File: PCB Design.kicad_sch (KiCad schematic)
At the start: 8 parts

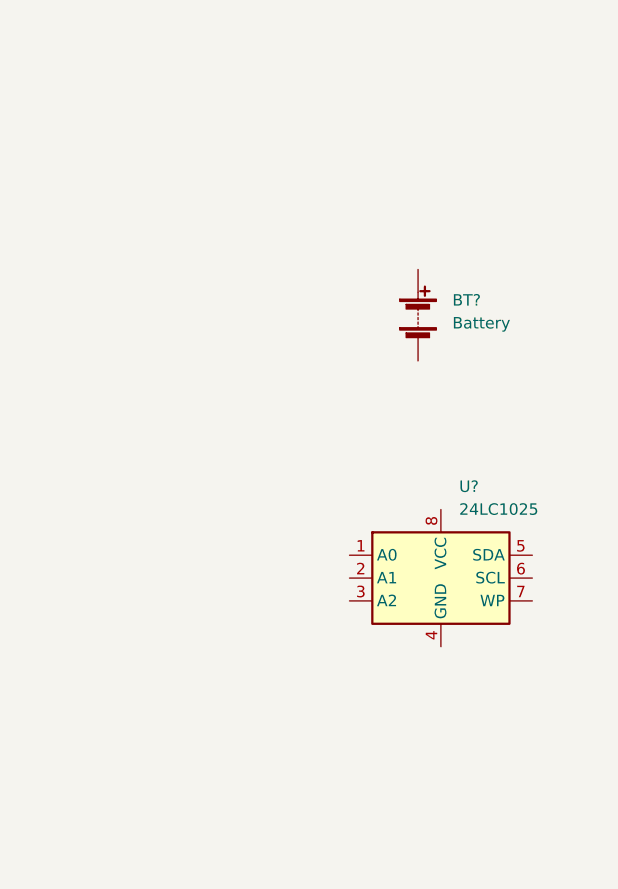
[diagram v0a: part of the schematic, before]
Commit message: add ATMEGA328P-AU from Digi-key library
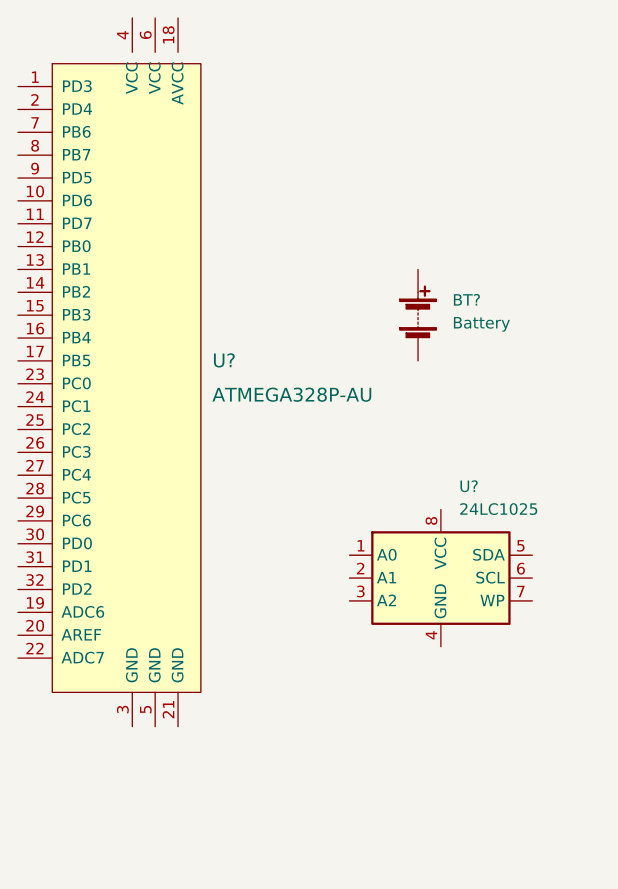
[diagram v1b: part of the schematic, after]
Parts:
- added U?: ATMEGA328P-AU, digikey-footprints:TQFP-32_7x7mm, symbol dk_Embedded-Microcontrollers:ATMEGA328P-AU
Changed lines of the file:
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@@
     (pin "8")
+  )
+  (symbol (lib_id "dk_Embedded-Microcontrollers:ATMEGA328P-AU") (at 52.07 92.71 0) (unit 1)
+    (in_bom yes) (on_board yes) (fields_autoplaced)
+    (property "Reference" "U?" (id 0) (at 60.96 90.17 0)
+      (effects (font (size 1.524 1.524)) (justify left))
+    )
+    (property "Value" "ATMEGA328P-AU" (id 1) (at 60.96 93.98 0)
+      (effects (font (size 1.524 1.524)) (justify left))
+    )
+    (property "Footprint" "digikey-footprints:TQFP-32_7x7mm" (id 2) (at 57.15 87.63 0)
+      (effects (font (size 1.524 1.524)) (justify left) hide)
+    )
+    (property "Datasheet" "http://www.microchip.com/mymicrochip/filehandler.aspx?ddocname=en608326" (id 3) (at 57.15 85.09 0)
+      (effects (font (size 1.524 1.524)) (justify left) hide)
+    )
+    (property "Digi-Key_PN" "ATMEGA328P-AU-ND" (id 4) (at 57.15 82.55 0)
+      (effects (font (size 1.524 1.524)) (justify left) hide)
+    )
+    (property "MPN" "ATMEGA328P-AU" (id 5) (at 57.15 80.01 0)
+      (effects (font (size 1.524 1.524)) (justify left) hide)
+    )
+    (property "Category" "Integrated Circuits (ICs)" (id 6) (at 57.15 77.47 0)
+      (effects (font (size 1.524 1.524)) (justify left) hide)
+    )
+    (property "Family" "Embedded - Microcontrollers" (id 7) (at 57.15 74.93 0)
+      (effects (font (size 1.524 1.524)) (justify left) hide)
+    )
+    (property "DK_Datasheet_Link" "http://www.microchip.com/mymicrochip/filehandler.aspx?ddocname=en608326" (id 8) (at 57.15 72.39 0)
+      (effects (font (size 1.524 1.524)) (justify left) hide)
+    )
+    (property "DK_Detail_Page" "/product-detail/en/microchip-technology/ATMEGA328P-AU/ATMEGA328P-AU-ND/1832260" (id 9) (at 57.15 69.85 0)
+      (effects (font (size 1.524 1.524)) (justify left) hide)
+    )
+    (property "Description" "IC MCU 8BIT 32KB FLASH 32TQFP" (id 10) (at 57.15 67.31 0)
+      (effects (font (size 1.524 1.524)) (justify left) hide)
+    )
+    (property "Manufacturer" "Microchip Technology" (id 11) (at 57.15 64.77 0)
+      (effects (font (size 1.524 1.524)) (justify left) hide)
+    )
+    (property "Status" "Active" (id 12) (at 57.15 62.23 0)
+      (effects (font (size 1.524 1.524)) (justify left) hide)
+    )
+    (pin "1")
+    (pin "10")
+    (pin "11")
+    (pin "12")
+    (pin "13")
+    (pin "14")
+    (pin "15")
+    (pin "16")
+    (pin "17")
+    (pin "18")
+    (pin "19")
+    (pin "2")
+    (pin "20")
+    (pin "21")
+    (pin "22")
+    (pin "23")
+    (pin "24")
+    (pin "25")
+    (pin "26")
+    (pin "27")
+    (pin "28")
+    (pin "29")
+    (pin "3")
+    (pin "30")
+    (pin "31")
+    (pin "32")
+    (pin "4")
+    (pin "5")
+    (pin "6")
+    (pin "7")
+    (pin "8")
+    (pin "9")
   )
   (symbol (lib_id "Device:LED") (at 205.74 77.47 0) (unit 1)
@@
       (reference "U?") (unit 1) (value "24LC1025") (footprint "")
     )
-  )
+    (path "/11816a99-511f-4707-8ba2-7dbc85864458"
+      (reference "U?") (unit 1) (value "ATMEGA328P-AU") (footprint "digikey-footprints:TQFP-32_7x7mm")
+    )
+  )

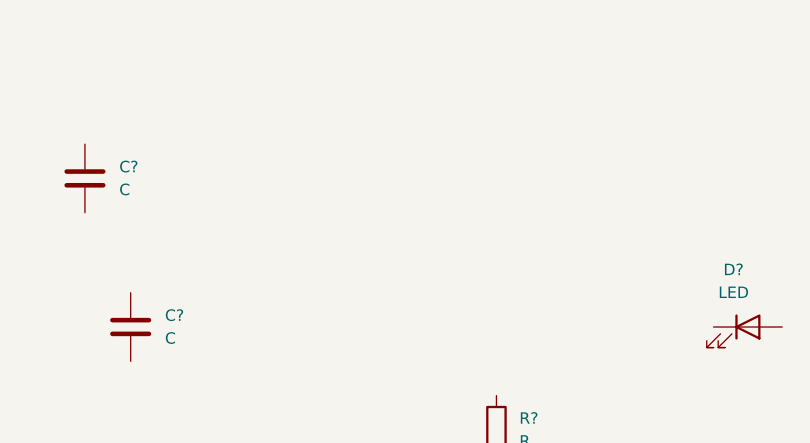
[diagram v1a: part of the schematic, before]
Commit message: add custom clock IC symbol
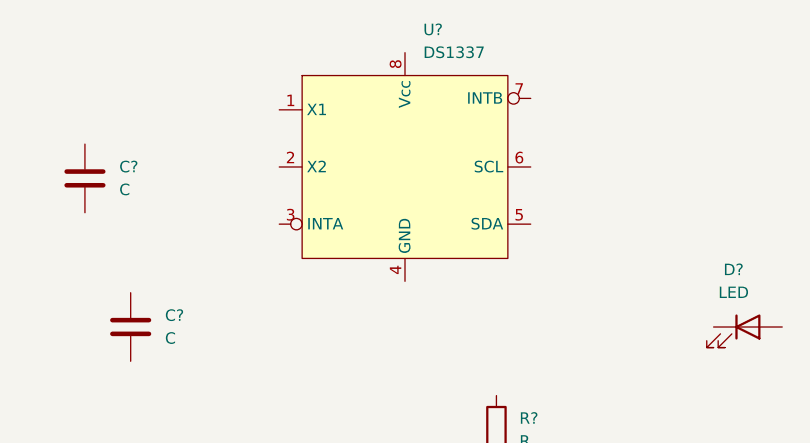
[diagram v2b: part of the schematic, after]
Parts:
- added U?: DS1337, symbol I2CRTC:DS1337
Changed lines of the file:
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@@
     (pin "2")
+  )
+  (symbol (lib_id "I2CRTC:DS1337") (at 167.64 59.69 0) (unit 1)
+    (in_bom yes) (on_board yes) (fields_autoplaced)
+    (property "Reference" "U?" (id 0) (at 169.6594 44.45 0)
+      (effects (font (size 1.27 1.27)) (justify left))
+    )
+    (property "Value" "DS1337" (id 1) (at 169.6594 46.99 0)
+      (effects (font (size 1.27 1.27)) (justify left))
+    )
+    (property "Footprint" "" (id 2) (at 167.64 59.69 0)
+      (effects (font (size 1.27 1.27)) hide)
+    )
+    (property "Datasheet" "" (id 3) (at 167.64 59.69 0)
+      (effects (font (size 1.27 1.27)) hide)
+    )
+    (pin "1")
+    (pin "2")
+    (pin "3")
+    (pin "4")
+    (pin "5")
+    (pin "6")
+    (pin "7")
+    (pin "8")
   )
   (symbol (lib_id "Device:C") (at 137.16 77.47 0) (unit 1)
@@
       (reference "U?") (unit 1) (value "ATMEGA328P-AU") (footprint "digikey-footprints:TQFP-32_7x7mm")
     )
+    (path "/b261580b-4179-4e44-80bf-c6d63aab43a1"
+      (reference "U?") (unit 1) (value "DS1337") (footprint "")
+    )
   )

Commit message: complete footprint association
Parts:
- added U2: 24LC1025, Package_SO:SOIC-8_5.23x5.23mm_P1.27mm, symbol Memory_EEPROM:24LC1025
- added Y1: Crystal 32MHz, Crystal:Crystal_SMD_MicroCrystal_CC7V-T1A-2Pin_3.2x1.5mm, symbol Device:Crystal
- added Y2: Crystal 16MHz, Crystal:Crystal_SMD_5032-2Pin_5.0x3.2mm_HandSoldering, symbol Device:Crystal
- BT1: renamed from BT?; value Battery -> Battery 3V; footprint (none) -> Connector_PinHeader_2.54mm:PinHeader_1x02_P2.54mm_Vertical
- C1, C2: renamed from C?; value C -> 22pF; footprint (none) -> Capacitor_SMD:C_0805_2012Metric_Pad1.18x1.45mm_HandSolder
- C3: renamed from C?; value C_Polarized -> 10uF; footprint (none) -> Capacitor_SMD:C_0805_2012Metric_Pad1.18x1.45mm_HandSolder
- D1: renamed from D?; footprint (none) -> LED_SMD:LED_0805_2012Metric_Pad1.15x1.40mm_HandSolder
- R1: renamed from R?; value R -> 330Ohm; footprint (none) -> Resistor_SMD:R_0805_2012Metric_Pad1.20x1.40mm_HandSolder
- R2: renamed from R?; value R -> 10KOhm; footprint (none) -> Resistor_SMD:R_0805_2012Metric_Pad1.20x1.40mm_HandSolder
- U1: renamed from U?; footprint (none) -> Package_SO:SOIC-8_5.23x5.23mm_P1.27mm
- U3: renamed from U?; footprint (none) -> Package_SO:SO-8_5.3x6.2mm_P1.27mm
- gave numbers to parts that had none: 1
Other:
- moved on the sheet: BT1, C1, C2, C3, D1, R1, R2, U1, U3, U4

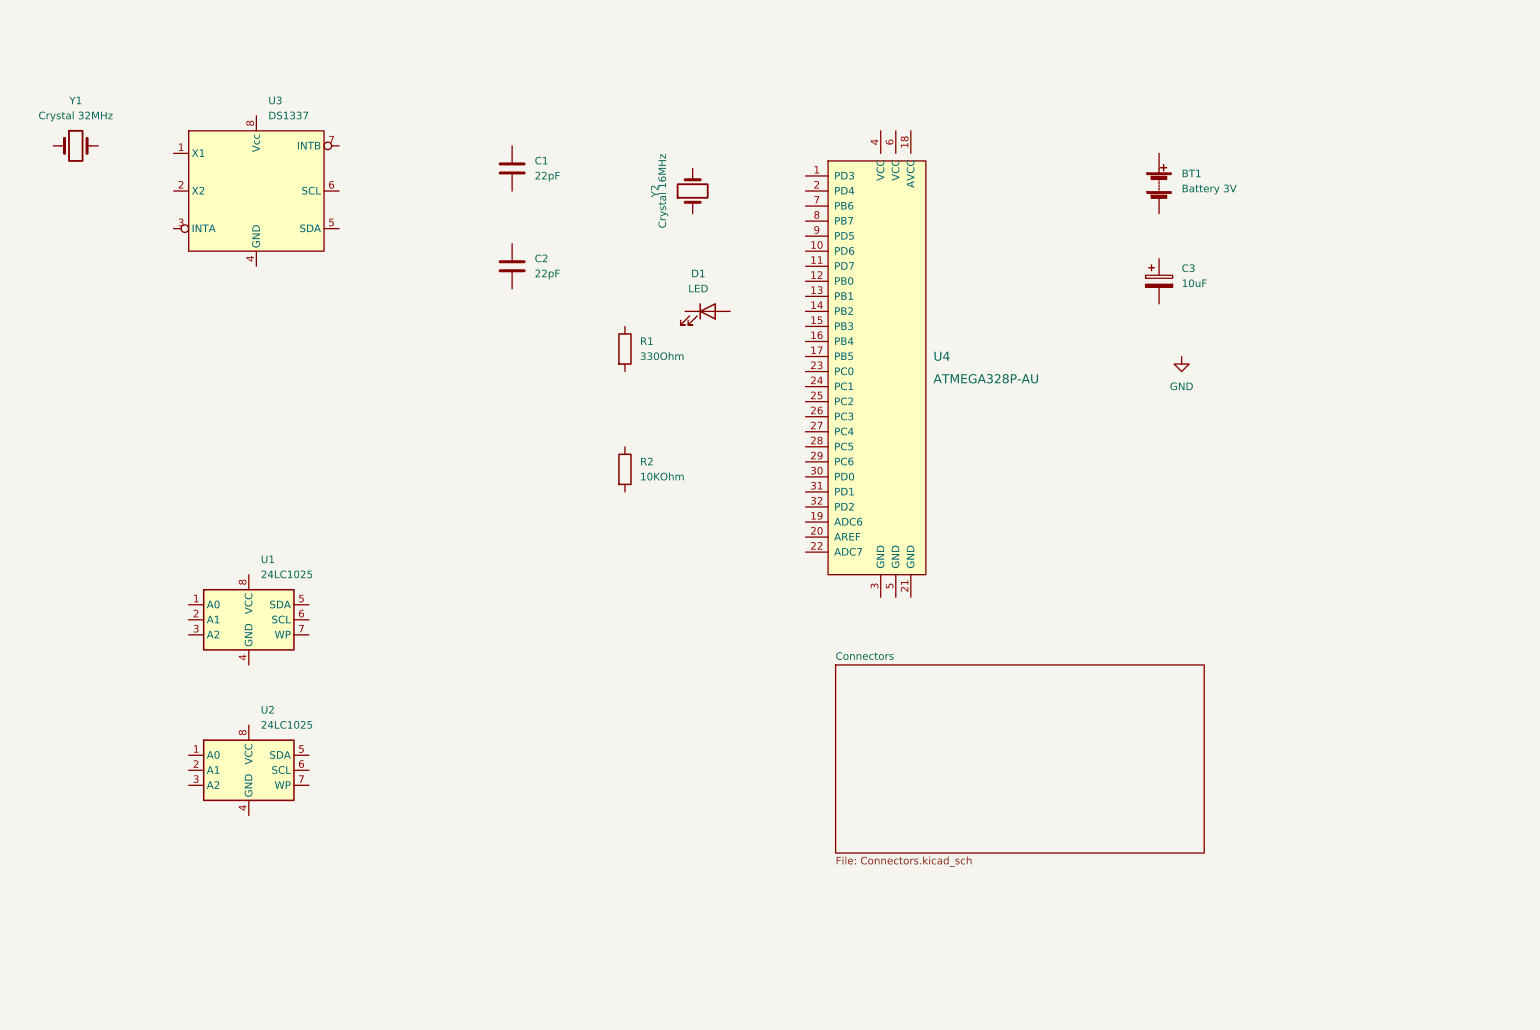
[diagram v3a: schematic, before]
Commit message: complete wiring in the root sheet
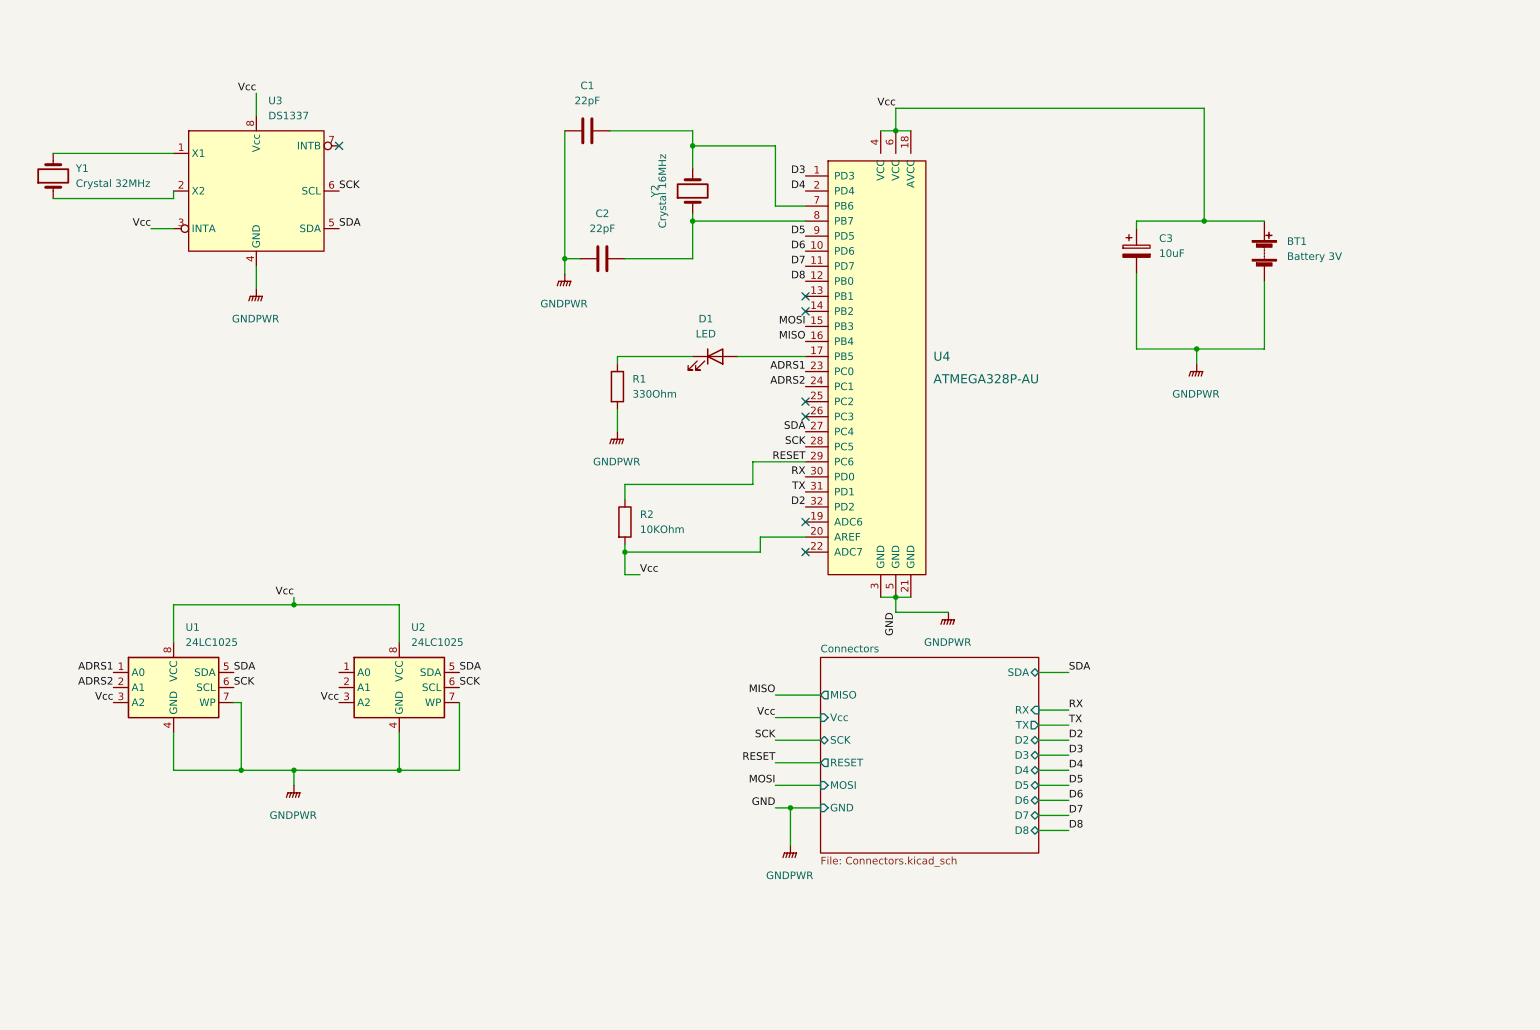
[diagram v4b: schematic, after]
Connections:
- net ADRS1: now reaches U1.1 (A0)
- net ADRS1: now also U4.23 (PC0)
- net ADRS2: now reaches U1.2 (A1)
- net ADRS2: now also U4.24 (PC1)
- net Vcc: now reaches U1.3 (A2)
- net Vcc: now also BT1.1 (+), C3.1, R2.2, U1.8 (VCC), U2.3 (A2), U2.8 (VCC), U3.3 (INTA), U3.8 (Vcc), U4.18 (AVCC), U4.20 (AREF), U4.4 (VCC), U4.6 (VCC)
- net GNDPWR: now reaches U1.4 (GND)
- net GNDPWR: now also BT1.2 (-), C1.1, C2.1, C3.2, R1.2, U1.7 (WP), U2.4 (GND), U2.7 (WP), U3.4 (GND), U4.21 (GND), U4.3 (GND), U4.5 (GND)
- net SDA: now reaches U1.5 (SDA)
- net SDA: now also U2.5 (SDA), U3.5 (SDA), U4.27 (PC4)
- net SCK: now reaches U1.6 (SCL)
- net SCK: now also U2.6 (SCL), U3.6 (SCL), U4.28 (PC5)
- net D3: now reaches U4.1 (PD3)
- net D6: now reaches U4.10 (PD6)
- net D7: now reaches U4.11 (PD7)
- net D8: now reaches U4.12 (PB0)
- net MOSI: now reaches U4.15 (PB3)
- net MISO: now reaches U4.16 (PB4)
- net at U4.17 (PB5): now also D1.2 (A)
- net D4: now reaches U4.2 (PD4)
- net RESET: now reaches U4.29 (PC6)
- net RESET: now also R2.1
- net RX: now reaches U4.30 (PD0)
- net TX: now reaches U4.31 (PD1)
- net D2: now reaches U4.32 (PD2)
- net at U4.7 (PB6): now also C1.2, Y2.2
- net at U4.8 (PB7): now also C2.2, Y2.1
- net D5: now reaches U4.9 (PD5)
- net at D1.1 (K): now also R1.1
- net at Y1.1: now also U3.2 (X2)
- net at Y1.2: now also U3.1 (X1)
- no-connect marks 0 -> 7
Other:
- sheet Connectors ports: added D2, D3, D4, D5, D6, D7, D8, GND, MISO, MOSI, RESET, RX, SCK, SDA, TX, Vcc; removed none
- moved on the sheet: BT1, C1, C2, C3, D1, R1, R2, U1, U2, Y1

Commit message: add functional block description
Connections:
- net ADRS1: now also U2.1 (A0)
- net ADRS2: now also U2.2 (A1)
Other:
- note added: "N1-Clock/Calendar"
- note added: "N2-ATMEGA328P-AU with Oscillator and Battery"
- note added: "N3-EEPROM"
- note added: "N4-Connectors"
- moved on the sheet: U1, U2
